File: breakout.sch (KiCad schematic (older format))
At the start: 10 parts, among them P1 CONN_01X08, P2 CONN_01X08, U1 ESP-12E, U2 APE8865Y5-33-HF-3

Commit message: Add pullup resistor to GPIO2.
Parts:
- added R6: 10KΩ, Resistors_SMD:R_0805_HandSoldering, symbol R
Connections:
- wire segments 41 -> 43
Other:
- moved on the sheet: R4
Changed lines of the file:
@@
 Title "ESP8266 breakout board"
 Date "2015-12-30"
-Rev "1.0"
+Rev "1.1"
 Comp "Stochastic Technologies"
 Comment1 ""
@@
 L R R4
 U 1 1 56840F5D
-P 6700 2300
-F 0 "R4" H 6770 2346 50  0000 L CNN
-F 1 "10KΩ" H 6770 2254 50  0000 L CNN
-F 2 "Resistors_SMD:R_0805_HandSoldering" V 6630 2300 50  0001 C CNN
-F 3 "" H 6700 2300 50  0000 C CNN
-	1    6700 2300
+P 6900 2300
+F 0 "R4" H 6970 2346 50  0000 L CNN
+F 1 "10KΩ" H 6970 2254 50  0000 L CNN
+F 2 "Resistors_SMD:R_0805_HandSoldering" V 6830 2300 50  0001 C CNN
+F 3 "" H 6900 2300 50  0000 C CNN
+	1    6900 2300
 	1    0    0    -1
 $EndComp
@@
 	6500 3650 7000 3650
 Wire Wire Line
-	3600 2050 6700 2050
+	3600 2050 6900 2050
 Wire Wire Line
 	3150 2400 3750 2400
@@
 Wire Wire Line
 	3150 4500 6800 4500
-Wire Wire Line
-	6700 2050 6700 2150
-Wire Wire Line
-	6700 2450 6700 3350
 Wire Wire Line
 	4250 2400 4250 3150
@@
 	3750 1500 3750 2100
 Connection ~ 3750 2050
-Connection ~ 6700 3350
 Wire Wire Line
 	6550 4500 6550 3650
@@
 Wire Wire Line
 	3300 1500 3750 1500
+$Comp
+L R R6
+U 1 1 56844D05
+P 6550 2300
+F 0 "R6" H 6620 2346 50  0000 L CNN
+F 1 "10KΩ" H 6620 2254 50  0000 L CNN
+F 2 "Resistors_SMD:R_0805_HandSoldering" V 6480 2300 50  0001 C CNN
+F 3 "" H 6550 2300 50  0000 C CNN
+	1    6550 2300
+	1    0    0    -1
+$EndComp
+Wire Wire Line
+	6900 2050 6900 2150
+Wire Wire Line
+	6550 2150 6550 2050
+Connection ~ 6550 2050
+Wire Wire Line
+	6550 2450 6550 3350
+Connection ~ 6550 3350
+Wire Wire Line
+	6900 2450 6900 3450
+Connection ~ 6900 3450
 $EndSCHEMATC

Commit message: Update images.
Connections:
- wire segments 43 -> 57
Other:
- moved on the sheet: C1, R1, R2, R3, R4, R5, R6, U2
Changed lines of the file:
@@
 L APE8865Y5-33-HF-3 U2
 U 1 1 56840629
-P 3150 2100
-F 0 "U2" H 3150 2510 50  0000 C CNN
-F 1 "APE8865Y5-33-HF-3" H 3150 2418 50  0000 C CNN
-F 2 "TO_SOT_Packages_SMD:SOT-23-5" H 3150 2326 50  0001 C CIN
-F 3 "" H 3150 2100 50  0000 C CNN
-	1    3150 2100
+P 3150 2200
+F 0 "U2" H 3150 2610 50  0000 C CNN
+F 1 "APE8865Y5-33-HF-3" H 3150 2518 50  0000 C CNN
+F 2 "TO_SOT_Packages_SMD:SOT-23-5" H 3150 2426 50  0001 C CIN
+F 3 "" H 3150 2200 50  0000 C CNN
+	1    3150 2200
 	1    0    0    -1
 $EndComp
@@
 L C C1
 U 1 1 56840717
-P 3750 2250
-F 0 "C1" H 3865 2342 50  0000 L CNN
-F 1 "1uF" H 3865 2250 50  0000 L CNN
-F 2 "Capacitors_SMD:C_0805_HandSoldering" H 3865 2158 50  0001 L CNN
-F 3 "" H 3750 2250 50  0000 C CNN
-	1    3750 2250
+P 3750 2350
+F 0 "C1" H 3865 2442 50  0000 L CNN
+F 1 "1uF" H 3865 2350 50  0000 L CNN
+F 2 "Capacitors_SMD:C_0805_HandSoldering" H 3865 2258 50  0001 L CNN
+F 3 "" H 3750 2350 50  0000 C CNN
+	1    3750 2350
 	1    0    0    -1
 $EndComp
@@
 L R R2
 U 1 1 56840960
-P 4600 2250
-F 0 "R2" H 4670 2296 50  0000 L CNN
-F 1 "10KΩ" H 4670 2204 50  0000 L CNN
-F 2 "Resistors_SMD:R_0805_HandSoldering" V 4530 2250 50  0001 C CNN
-F 3 "" H 4600 2250 50  0000 C CNN
-	1    4600 2250
+P 4600 2500
+F 0 "R2" H 4670 2546 50  0000 L CNN
+F 1 "10KΩ" H 4670 2454 50  0000 L CNN
+F 2 "Resistors_SMD:R_0805_HandSoldering" V 4530 2500 50  0001 C CNN
+F 3 "" H 4600 2500 50  0000 C CNN
+	1    4600 2500
 	1    0    0    -1
 $EndComp
@@
 L R R1
 U 1 1 56840F07
-P 4250 2250
-F 0 "R1" H 4320 2296 50  0000 L CNN
-F 1 "10KΩ" H 4320 2204 50  0000 L CNN
-F 2 "Resistors_SMD:R_0805_HandSoldering" V 4180 2250 50  0001 C CNN
-F 3 "" H 4250 2250 50  0000 C CNN
-	1    4250 2250
+P 4250 2500
+F 0 "R1" H 4320 2546 50  0000 L CNN
+F 1 "10KΩ" H 4320 2454 50  0000 L CNN
+F 2 "Resistors_SMD:R_0805_HandSoldering" V 4180 2500 50  0001 C CNN
+F 3 "" H 4250 2500 50  0000 C CNN
+	1    4250 2500
 	1    0    0    -1
 $EndComp
@@
 L R R4
 U 1 1 56840F5D
-P 6900 2300
-F 0 "R4" H 6970 2346 50  0000 L CNN
-F 1 "10KΩ" H 6970 2254 50  0000 L CNN
-F 2 "Resistors_SMD:R_0805_HandSoldering" V 6830 2300 50  0001 C CNN
-F 3 "" H 6900 2300 50  0000 C CNN
-	1    6900 2300
+P 6900 2500
+F 0 "R4" H 6970 2546 50  0000 L CNN
+F 1 "10KΩ" H 6970 2454 50  0000 L CNN
+F 2 "Resistors_SMD:R_0805_HandSoldering" V 6830 2500 50  0001 C CNN
+F 3 "" H 6900 2500 50  0000 C CNN
+	1    6900 2500
 	1    0    0    -1
 $EndComp
@@
 L R R3
 U 1 1 568411DE
-P 6800 4050
-F 0 "R3" H 6870 4096 50  0000 L CNN
-F 1 "10KΩ" H 6870 4004 50  0000 L CNN
-F 2 "Resistors_SMD:R_0805_HandSoldering" V 6730 4050 50  0001 C CNN
-F 3 "" H 6800 4050 50  0000 C CNN
-	1    6800 4050
-	1    0    0    -1
-$EndComp
-Wire Wire Line
-	3800 2950 4700 2950
+P 6800 3900
+F 0 "R3" H 6870 3946 50  0000 L CNN
+F 1 "10KΩ" H 6870 3854 50  0000 L CNN
+F 2 "Resistors_SMD:R_0805_HandSoldering" V 6730 3900 50  0001 C CNN
+F 3 "" H 6800 3900 50  0000 C CNN
+	1    6800 3900
+	1    0    0    -1
+$EndComp
+Wire Wire Line
+	3800 2950 4600 2950
+Wire Wire Line
+	4600 2950 4700 2950
 Wire Wire Line
 	4700 3050 3800 3050
 Wire Wire Line
-	3800 3150 4700 3150
+	3800 3150 4250 3150
+Wire Wire Line
+	4250 3150 4700 3150
 Wire Wire Line
 	4700 3250 3800 3250
@@
 	6500 3250 7000 3250
 Wire Wire Line
-	6500 3350 7000 3350
-Wire Wire Line
-	6500 3450 7000 3450
-Wire Wire Line
-	6500 3550 7000 3550
-Wire Wire Line
-	6500 3650 7000 3650
-Wire Wire Line
-	3600 2050 6900 2050
-Wire Wire Line
-	3150 2400 3750 2400
-Wire Wire Line
-	3150 2400 3150 4500
-Wire Wire Line
-	3150 4500 6800 4500
-Wire Wire Line
-	4250 2400 4250 3150
+	6500 3350 6550 3350
+Wire Wire Line
+	6550 3350 7000 3350
+Wire Wire Line
+	6500 3450 6900 3450
+Wire Wire Line
+	6900 3450 7000 3450
+Wire Wire Line
+	6500 3550 6800 3550
+Wire Wire Line
+	6800 3550 7000 3550
+Wire Wire Line
+	6500 3650 6550 3650
+Wire Wire Line
+	6550 3650 7000 3650
+Wire Wire Line
+	3600 2150 3750 2150
+Wire Wire Line
+	3750 2150 4100 2150
+Wire Wire Line
+	4100 2150 4250 2150
+Wire Wire Line
+	4250 2150 4600 2150
+Wire Wire Line
+	4600 2150 6550 2150
+Wire Wire Line
+	6550 2150 6900 2150
+Wire Wire Line
+	3150 2500 3750 2500
+Wire Wire Line
+	3150 2500 3150 4250
+Wire Wire Line
+	3150 4250 6550 4250
+Wire Wire Line
+	6550 4250 6800 4250
+Wire Wire Line
+	4250 2650 4250 3150
 Connection ~ 4250 3150
 Wire Wire Line
-	4600 2400 4600 2950
+	4600 2650 4600 2950
 Connection ~ 4600 2950
 Wire Wire Line
-	4250 2100 4250 2050
-Connection ~ 4250 2050
-Wire Wire Line
-	4600 2050 4600 2100
-Connection ~ 4600 2050
-Wire Wire Line
-	3750 1500 3750 2100
-Connection ~ 3750 2050
-Wire Wire Line
-	6550 4500 6550 3650
+	4250 2350 4250 2150
+Connection ~ 4250 2150
+Wire Wire Line
+	4600 2150 4600 2350
+Connection ~ 4600 2150
+Wire Wire Line
+	3750 1650 3750 2150
+Wire Wire Line
+	3750 2150 3750 2200
+Connection ~ 3750 2150
+Wire Wire Line
+	6550 4250 6550 3650
 Connection ~ 6550 3650
 Wire Wire Line
-	6800 3550 6800 3900
+	6800 3550 6800 3750
 Connection ~ 6800 3550
 Wire Wire Line
-	6800 4500 6800 4200
-Connection ~ 6550 4500
+	6800 4250 6800 4050
+Connection ~ 6550 4250
 Wire Wire Line
 	4700 3650 4100 3650
 Wire Wire Line
-	4100 3650 4100 2050
-Connection ~ 4100 2050
+	4100 3650 4100 2150
+Connection ~ 4100 2150
 Wire Wire Line
 	3800 3650 3800 3850
@@
 	3800 3850 2500 3850
 Wire Wire Line
-	2500 3850 2500 2050
-Wire Wire Line
-	2500 2050 2700 2050
+	2500 3850 2500 2150
+Wire Wire Line
+	2500 2150 2600 2150
+Wire Wire Line
+	2600 2150 2700 2150
 $Comp
 L +12V #PWR01
 U 1 1 56841BDC
-P 2500 2050
-F 0 "#PWR01" H 2500 1900 50  0001 C CNN
-F 1 "+12V" V 2518 2177 50  0000 L CNN
-F 2 "" H 2500 2050 50  0000 C CNN
-F 3 "" H 2500 2050 50  0000 C CNN
-	1    2500 2050
+P 2500 2150
+F 0 "#PWR01" H 2500 2000 50  0001 C CNN
+F 1 "+12V" V 2518 2277 50  0000 L CNN
+F 2 "" H 2500 2150 50  0000 C CNN
+F 3 "" H 2500 2150 50  0000 C CNN
+	1    2500 2150
 	0    -1   -1   0
 $EndComp
@@
 L GND #PWR02
 U 1 1 56841C6C
-P 6800 4500
-F 0 "#PWR02" H 6800 4250 50  0001 C CNN
-F 1 "GND" H 6808 4326 50  0000 C CNN
-F 2 "" H 6800 4500 50  0000 C CNN
-F 3 "" H 6800 4500 50  0000 C CNN
-	1    6800 4500
+P 6800 4250
+F 0 "#PWR02" H 6800 4000 50  0001 C CNN
+F 1 "GND" H 6808 4076 50  0000 C CNN
+F 2 "" H 6800 4250 50  0000 C CNN
+F 3 "" H 6800 4250 50  0000 C CNN
+	1    6800 4250
 	1    0    0    -1
 $EndComp
@@
 Wire Wire Line
 	1650 2050 1650 2250
-NoConn ~ 3600 2200
-Wire Wire Line
-	2700 2050 2700 2200
-Text Label 5100 2050 0    60   ~ 0
+NoConn ~ 3600 2300
+Wire Wire Line
+	2700 2150 2700 2300
+Text Label 5100 2150 0    60   ~ 0
 3V3
 $Comp
 L R R5
 U 1 1 56842AB4
-P 3150 1500
-F 0 "R5" V 3358 1500 50  0000 C CNN
-F 1 "0Ω" V 3266 1500 50  0000 C CNN
-F 2 "Resistors_SMD:R_0805_HandSoldering" V 3080 1500 50  0001 C CNN
-F 3 "" H 3150 1500 50  0000 C CNN
-	1    3150 1500
+P 3150 1650
+F 0 "R5" V 3358 1650 50  0000 C CNN
+F 1 "0Ω" V 3266 1650 50  0000 C CNN
+F 2 "Resistors_SMD:R_0805_HandSoldering" V 3080 1650 50  0001 C CNN
+F 3 "" H 3150 1650 50  0000 C CNN
+	1    3150 1650
 	0    -1   -1   0
 $EndComp
 Wire Wire Line
-	3000 1500 2600 1500
-Wire Wire Line
-	2600 1500 2600 2050
-Connection ~ 2600 2050
-Wire Wire Line
-	3300 1500 3750 1500
+	3000 1650 2600 1650
+Wire Wire Line
+	2600 1650 2600 2150
+Connection ~ 2600 2150
+Wire Wire Line
+	3300 1650 3750 1650
 $Comp
 L R R6
 U 1 1 56844D05
-P 6550 2300
-F 0 "R6" H 6620 2346 50  0000 L CNN
-F 1 "10KΩ" H 6620 2254 50  0000 L CNN
-F 2 "Resistors_SMD:R_0805_HandSoldering" V 6480 2300 50  0001 C CNN
-F 3 "" H 6550 2300 50  0000 C CNN
-	1    6550 2300
-	1    0    0    -1
-$EndComp
-Wire Wire Line
-	6900 2050 6900 2150
-Wire Wire Line
-	6550 2150 6550 2050
-Connection ~ 6550 2050
-Wire Wire Line
-	6550 2450 6550 3350
+P 6550 2500
+F 0 "R6" H 6620 2546 50  0000 L CNN
+F 1 "10KΩ" H 6620 2454 50  0000 L CNN
+F 2 "Resistors_SMD:R_0805_HandSoldering" V 6480 2500 50  0001 C CNN
+F 3 "" H 6550 2500 50  0000 C CNN
+	1    6550 2500
+	1    0    0    -1
+$EndComp
+Wire Wire Line
+	6900 2150 6900 2350
+Wire Wire Line
+	6550 2350 6550 2150
+Connection ~ 6550 2150
+Wire Wire Line
+	6550 2650 6550 3350
 Connection ~ 6550 3350
 Wire Wire Line
-	6900 2450 6900 3450
+	6900 2650 6900 3450
 Connection ~ 6900 3450
 $EndSCHEMATC

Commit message: Add pin.
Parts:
- removed P1, P2: CONN_01X08, Pin_Headers:Pin_Header_Straight_1x08, symbol CONN_01X08
- removed R5: 0Ω, Resistors_SMD:R_0805_HandSoldering, symbol R
- added P1, P2: CONN_01X09, Pin_Headers:Pin_Header_Straight_1x09, symbol CONN_01X09
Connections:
- wire segments 57 -> 45
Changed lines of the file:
@@
-	1    0    0    -1
-$EndComp
-$Comp
-L CONN_01X08 P1
-U 1 1 5683F38F
-P 3600 3300
-F 0 "P1" H 3678 3384 50  0000 L CNN
-F 1 "CONN_01X08" H 3678 3292 50  0000 L CNN
-F 2 "Pin_Headers:Pin_Header_Straight_1x08" H 3678 3200 50  0001 L CNN
-F 3 "" H 3600 3300 50  0000 C CNN
-	1    3600 3300
-	-1   0    0    -1
-$EndComp
-$Comp
-L CONN_01X08 P2
-U 1 1 5683F5C1
-P 7200 3300
-F 0 "P2" H 7277 3338 50  0000 L CNN
-F 1 "CONN_01X08" H 7277 3246 50  0000 L CNN
-F 2 "Pin_Headers:Pin_Header_Straight_1x08" H 7200 3300 50  0001 C CNN
-F 3 "" H 7200 3300 50  0000 C CNN
-	1    7200 3300
 	1    0    0    -1
 $EndComp
@@
 $EndComp
 Wire Wire Line
-	3800 2950 4600 2950
-Wire Wire Line
-	4600 2950 4700 2950
+	3800 2950 4700 2950
 Wire Wire Line
 	4700 3050 3800 3050
 Wire Wire Line
-	3800 3150 4250 3150
-Wire Wire Line
-	4250 3150 4700 3150
+	3800 3150 4700 3150
 Wire Wire Line
 	4700 3250 3800 3250
@@
 	6500 3250 7000 3250
 Wire Wire Line
-	6500 3350 6550 3350
-Wire Wire Line
-	6550 3350 7000 3350
-Wire Wire Line
-	6500 3450 6900 3450
-Wire Wire Line
-	6900 3450 7000 3450
-Wire Wire Line
-	6500 3550 6800 3550
-Wire Wire Line
-	6800 3550 7000 3550
-Wire Wire Line
-	6500 3650 6550 3650
-Wire Wire Line
-	6550 3650 7000 3650
-Wire Wire Line
-	3600 2150 3750 2150
-Wire Wire Line
-	3750 2150 4100 2150
-Wire Wire Line
-	4100 2150 4250 2150
-Wire Wire Line
-	4250 2150 4600 2150
-Wire Wire Line
-	4600 2150 6550 2150
-Wire Wire Line
-	6550 2150 6900 2150
+	6500 3350 7000 3350
+Wire Wire Line
+	6500 3450 7000 3450
+Wire Wire Line
+	6500 3550 7000 3550
+Wire Wire Line
+	6500 3650 7000 3650
+Wire Wire Line
+	3600 2150 6900 2150
 Wire Wire Line
 	3150 2500 3750 2500
@@
 	3150 2500 3150 4250
 Wire Wire Line
-	3150 4250 6550 4250
-Wire Wire Line
-	6550 4250 6800 4250
+	3150 4250 6800 4250
 Wire Wire Line
 	4250 2650 4250 3150
@@
 Connection ~ 4600 2150
 Wire Wire Line
-	3750 1650 3750 2150
-Wire Wire Line
-	3750 2150 3750 2200
-Connection ~ 3750 2150
-Wire Wire Line
 	6550 4250 6550 3650
 Connection ~ 6550 3650
@@
 Connection ~ 4100 2150
 Wire Wire Line
-	3800 3650 3800 3850
-Wire Wire Line
-	3800 3850 2500 3850
+	2500 3850 3900 3850
 Wire Wire Line
 	2500 3850 2500 2150
 Wire Wire Line
-	2500 2150 2600 2150
-Wire Wire Line
-	2600 2150 2700 2150
+	2500 2150 2700 2150
 $Comp
 L +12V #PWR01
@@
 3V3
 $Comp
-L R R5
-U 1 1 56842AB4
-P 3150 1650
-F 0 "R5" V 3358 1650 50  0000 C CNN
-F 1 "0Ω" V 3266 1650 50  0000 C CNN
-F 2 "Resistors_SMD:R_0805_HandSoldering" V 3080 1650 50  0001 C CNN
-F 3 "" H 3150 1650 50  0000 C CNN
-	1    3150 1650
-	0    -1   -1   0
-$EndComp
-Wire Wire Line
-	3000 1650 2600 1650
-Wire Wire Line
-	2600 1650 2600 2150
-Connection ~ 2600 2150
-Wire Wire Line
-	3300 1650 3750 1650
-$Comp
 L R R6
 U 1 1 56844D05
@@
 	6900 2650 6900 3450
 Connection ~ 6900 3450
+$Comp
+L CONN_01X09 P1
+U 1 1 568C725D
+P 3600 3350
+F 0 "P1" H 3600 3850 50  0000 C CNN
+F 1 "CONN_01X09" V 3700 3350 50  0000 C CNN
+F 2 "Pin_Headers:Pin_Header_Straight_1x09" H 3600 3350 50  0001 C CNN
+F 3 "" H 3600 3350 50  0000 C CNN
+	1    3600 3350
+	-1   0    0    -1
+$EndComp
+Wire Wire Line
+	3900 3850 3900 3650
+Wire Wire Line
+	3900 3650 3800 3650
+Wire Wire Line
+	3800 3750 4200 3750
+Wire Wire Line
+	4200 3750 4200 3650
+Connection ~ 4200 3650
+Wire Wire Line
+	3750 2200 3750 2150
+Connection ~ 3750 2150
+$Comp
+L CONN_01X09 P2
+U 1 1 568C7A2E
+P 7200 3350
+F 0 "P2" H 7200 3850 50  0000 C CNN
+F 1 "CONN_01X09" V 7300 3350 50  0000 C CNN
+F 2 "Pin_Headers:Pin_Header_Straight_1x09" H 7200 3350 50  0001 C CNN
+F 3 "" H 7200 3350 50  0000 C CNN
+	1    7200 3350
+	1    0    0    -1
+$EndComp
+Wire Wire Line
+	6900 3650 6900 3750
+Wire Wire Line
+	6900 3750 7000 3750
+Connection ~ 6900 3650
 $EndSCHEMATC

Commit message: Rewire everything.
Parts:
- U2: value APE8865Y5-33-HF-3 -> SPX3819M5-L-3-3 TR
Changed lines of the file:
@@
 P 3150 2200
 F 0 "U2" H 3150 2610 50  0000 C CNN
-F 1 "APE8865Y5-33-HF-3" H 3150 2518 50  0000 C CNN
+F 1 "SPX3819M5-L-3-3 TR" H 3150 2518 50  0000 C CNN
 F 2 "TO_SOT_Packages_SMD:SOT-23-5" H 3150 2426 50  0001 C CIN
 F 3 "" H 3150 2200 50  0000 C CNN

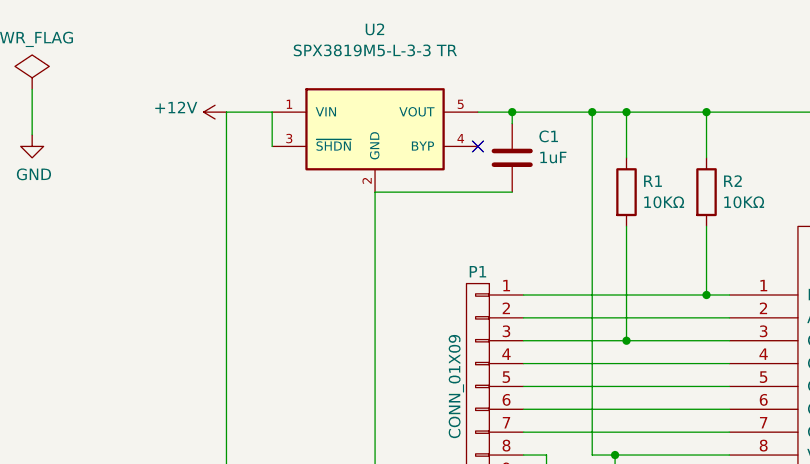
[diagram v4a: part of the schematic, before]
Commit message: Change to HT7333 regulator.
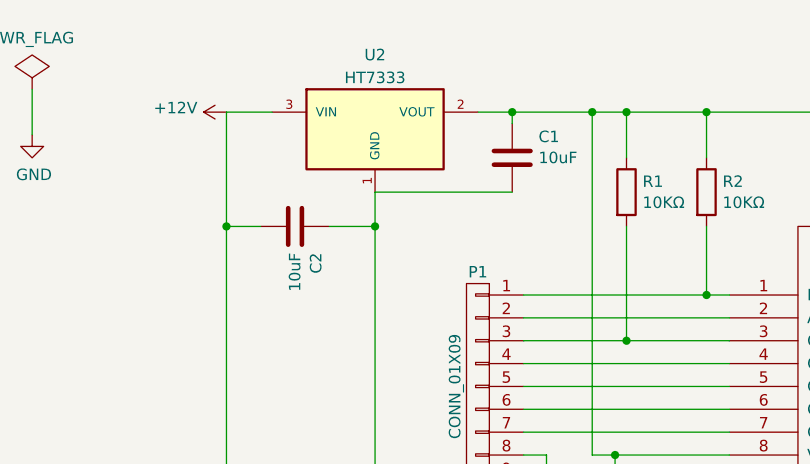
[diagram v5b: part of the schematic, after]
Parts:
- removed U2: SPX3819M5-L-3-3 TR, TO_SOT_Packages_SMD:SOT-23-5, symbol APE8865Y5-33-HF-3
- added C2: 10uF, Capacitors_SMD:C_0805_HandSoldering, symbol C
- added U2: HT7333, TO_SOT_Packages_SMD:SOT89-3_Housing_Handsoldering, symbol APE8865N-33-HF-3
- C1: value 1uF -> 10uF
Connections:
- net +12V: now also C2.2, U2.3 (VIN)
- net 3V3: now also U2.2 (VOUT)
- net GND: now also C2.1, U2.1 (GND)
- no-connect marks 7 -> 6
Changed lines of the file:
@@
 LIBS:valves
 LIBS:ESP8266
+LIBS:misc
 LIBS:breakout-cache
 EELAYER 25 0
@@
 NoConn ~ 5850 4150
 $Comp
-L APE8865Y5-33-HF-3 U2
-U 1 1 56840629
-P 3150 2200
-F 0 "U2" H 3150 2610 50  0000 C CNN
-F 1 "SPX3819M5-L-3-3 TR" H 3150 2518 50  0000 C CNN
-F 2 "TO_SOT_Packages_SMD:SOT-23-5" H 3150 2426 50  0001 C CIN
-F 3 "" H 3150 2200 50  0000 C CNN
-	1    3150 2200
-	1    0    0    -1
-$EndComp
-$Comp
 L C C1
 U 1 1 56840717
 P 3750 2350
 F 0 "C1" H 3865 2442 50  0000 L CNN
-F 1 "1uF" H 3865 2350 50  0000 L CNN
+F 1 "10uF" H 3865 2350 50  0000 L CNN
 F 2 "Capacitors_SMD:C_0805_HandSoldering" H 3865 2258 50  0001 L CNN
 F 3 "" H 3750 2350 50  0000 C CNN
@@
 	2500 2150 2700 2150
 $Comp
-L +12V #PWR01
+L +12V #PWR3
 U 1 1 56841BDC
 P 2500 2150
-F 0 "#PWR01" H 2500 2000 50  0001 C CNN
+F 0 "#PWR3" H 2500 2000 50  0001 C CNN
 F 1 "+12V" V 2518 2277 50  0000 L CNN
 F 2 "" H 2500 2150 50  0000 C CNN
@@
 $EndComp
 $Comp
-L GND #PWR02
+L GND #PWR4
 U 1 1 56841C6C
 P 6800 4250
-F 0 "#PWR02" H 6800 4000 50  0001 C CNN
+F 0 "#PWR4" H 6800 4000 50  0001 C CNN
 F 1 "GND" H 6808 4076 50  0000 C CNN
 F 2 "" H 6800 4250 50  0000 C CNN
@@
 $EndComp
 $Comp
-L PWR_FLAG #FLG03
+L PWR_FLAG #FLG1
 U 1 1 56841CB3
 P 1200 2200
-F 0 "#FLG03" H 1200 2295 50  0001 C CNN
+F 0 "#FLG1" H 1200 2295 50  0001 C CNN
 F 1 "PWR_FLAG" H 1200 2423 50  0000 C CNN
 F 2 "" H 1200 2200 50  0000 C CNN
@@
 $EndComp
 $Comp
-L PWR_FLAG #FLG04
+L PWR_FLAG #FLG2
 U 1 1 56841D0E
 P 1650 2050
-F 0 "#FLG04" H 1650 2145 50  0001 C CNN
+F 0 "#FLG2" H 1650 2145 50  0001 C CNN
 F 1 "PWR_FLAG" H 1650 2274 50  0000 C CNN
 F 2 "" H 1650 2050 50  0000 C CNN
@@
 $EndComp
 $Comp
-L +12V #PWR05
+L +12V #PWR1
 U 1 1 56841D46
 P 1200 2000
-F 0 "#PWR05" H 1200 1850 50  0001 C CNN
+F 0 "#PWR1" H 1200 1850 50  0001 C CNN
 F 1 "+12V" H 1218 2174 50  0000 C CNN
 F 2 "" H 1200 2000 50  0000 C CNN
@@
 	1200 2000 1200 2200
 $Comp
-L GND #PWR06
+L GND #PWR2
 U 1 1 56841DA6
 P 1650 2250
-F 0 "#PWR06" H 1650 2000 50  0001 C CNN
+F 0 "#PWR2" H 1650 2000 50  0001 C CNN
 F 1 "GND" H 1658 2076 50  0000 C CNN
 F 2 "" H 1650 2250 50  0000 C CNN
@@
 Wire Wire Line
 	1650 2050 1650 2250
-NoConn ~ 3600 2300
-Wire Wire Line
-	2700 2150 2700 2300
 Text Label 5100 2150 0    60   ~ 0
 3V3
@@
 	6900 3750 7000 3750
 Connection ~ 6900 3650
+$Comp
+L C C2
+U 1 1 5694F907
+P 2800 2650
+F 0 "C2" H 2915 2742 50  0000 L CNN
+F 1 "10uF" H 2915 2650 50  0000 L CNN
+F 2 "Capacitors_SMD:C_0805_HandSoldering" H 2915 2558 50  0001 L CNN
+F 3 "" H 2800 2650 50  0000 C CNN
+	1    2800 2650
+	0    1    1    0
+$EndComp
+Wire Wire Line
+	2650 2650 2500 2650
+Connection ~ 2500 2650
+Wire Wire Line
+	2950 2650 3150 2650
+Connection ~ 3150 2650
+$Comp
+L APE8865N-33-HF-3 U2
+U 1 1 5694FDB4
+P 3150 2200
+F 0 "U2" H 3150 2500 50  0000 C CNN
+F 1 "HT7333" H 3150 2400 50  0000 C CNN
+F 2 "TO_SOT_Packages_SMD:SOT89-3_Housing_Handsoldering" H 3150 2300 50  0001 C CIN
+F 3 "" H 3150 2200 50  0000 C CNN
+	1    3150 2200
+	1    0    0    -1
+$EndComp
 $EndSCHEMATC
